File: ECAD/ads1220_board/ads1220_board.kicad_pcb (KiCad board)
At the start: 4 copper layers, 38 x 24 mm, 32 parts, among them J2 LOAD CELL, J3 Conn_01x08, U1 TPS79301-EP, U3 ADS1220xPW, U4 OPA333xxDBV

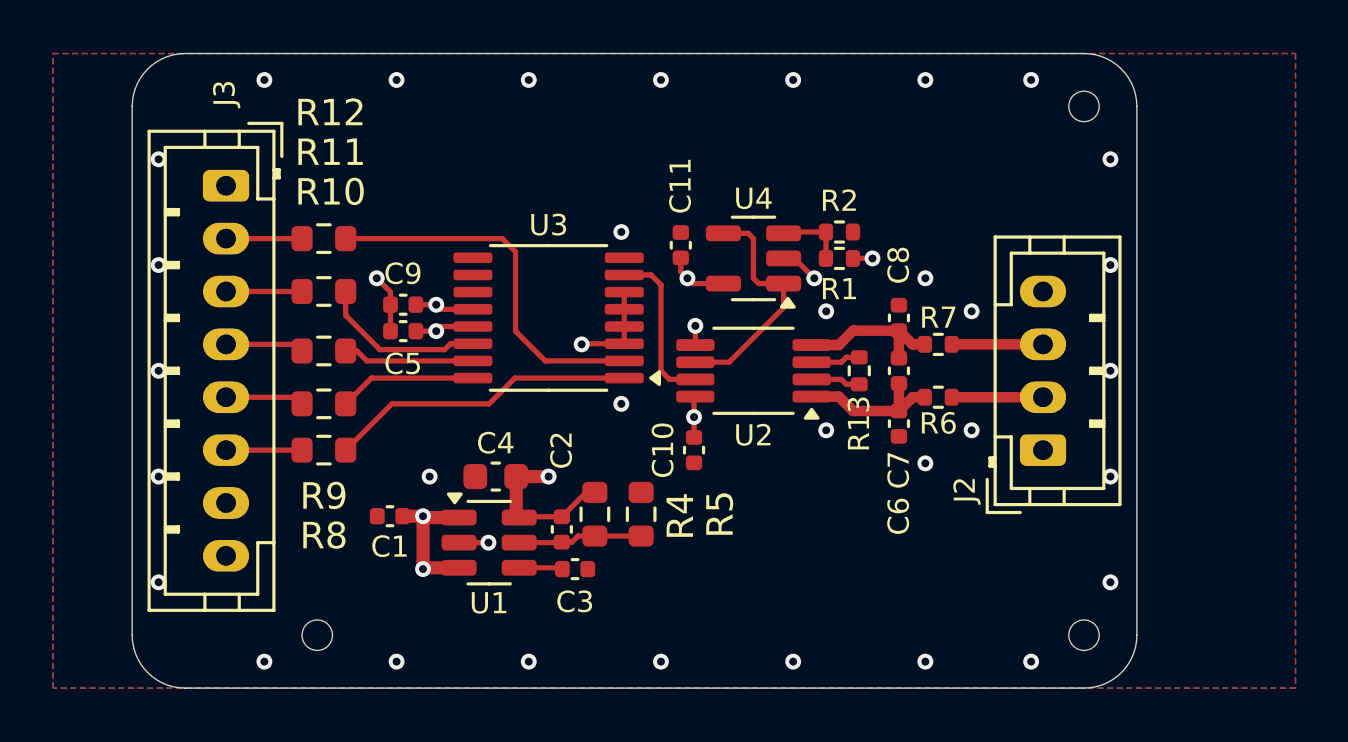
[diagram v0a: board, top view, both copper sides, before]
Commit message: update ads1220 schematic
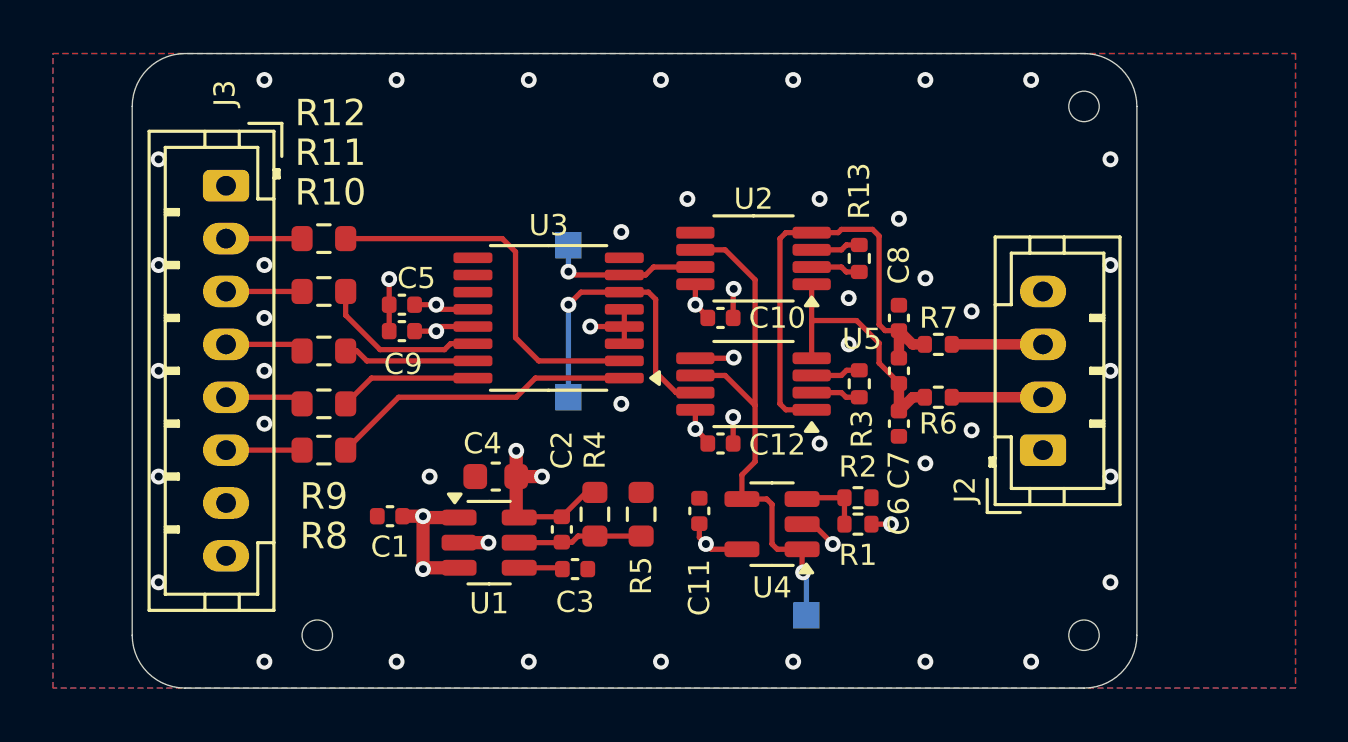
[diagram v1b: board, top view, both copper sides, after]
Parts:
- added C12: 0.1uF, Capacitor_SMD:C_0402_1005Metric, F.Cu at (132.2, 84.8)
- added R3: 220R, Resistor_SMD:R_0402_1005Metric, F.Cu at (137.5, 82.5)
- added TP1: TestPoint, TestPoint:TestPoint_Pad_1.0x1.0mm, B.Cu at (126.5, 77.2)
- added TP2: TestPoint, TestPoint:TestPoint_Pad_1.0x1.0mm, B.Cu at (126.5, 83.0)
- added TP3: TestPoint, TestPoint:TestPoint_Pad_1.0x1.0mm, B.Cu at (135.5, 91.2)
- added U5: ~, Package_SO:Texas_S-PDSO-G8_3x3mm_P0.65mm, F.Cu at (133.5, 82.5)
- moved C11 10.1 mm to (131.4, 87.3)
- moved R1 10.1 mm to (137.4, 87.8)
- moved R2 10.1 mm to (137.4, 86.8)
- moved U4 10.1 mm to (134.2, 87.8)
- moved C10 5.10 mm to (132.2, 80.0), turned to 180 degrees
- moved R13 4.25 mm to (137.5, 77.8)
- moved U2 4.25 mm to (133.5, 77.8)
- moved C5 1.00 mm to (120.2, 79.5)
- moved C9 1.00 mm to (120.2, 80.5)
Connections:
- C9 pad 2: +4V -> +3V3
- U3 pad 13: +4V -> +3V3
- U3 pad 6: GND -> /SIG_AMP-
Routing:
- net +3V3: track 0.00 -> 12.9 mm, vias 0 -> 1
- net /SIG_FLTR-: track 5.76 -> 18.0 mm
- net /INA_REF: track 9.05 -> 20.5 mm, vias 0 -> 1
- net /SIG_AMP-: track 0.00 -> 11.3 mm, vias 0 -> 1
- net /SIG_FLTR+: track 5.76 -> 9.75 mm
- net Net-(R3-Pad2): track 0.00 -> 1.88 mm
- net Net-(R3-Pad1): track 0.00 -> 1.87 mm
- net GND: track 9.10 -> 10.7 mm, vias 38 -> 48
- net /SIG_AMP+: track 6.23 -> 5.98 mm, vias 0 -> 1
- net +4V: track 15.5 -> 15.3 mm, vias 6 -> 7
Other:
- board text added: "ADC: ADS1220 REG: TPS791 INST_AMP: INA827 OP_AMP: OPA333"
- board text added: "INS_REF"
- board text added: "LOAD CELL"
- board text added: "REV B T.W."
- board text added: "SIG_AMP+"
- board text added: "SIG_AMP-"
- board text removed: "LOAD CELL ADC: ADS1220 REG: TPS791 INST_AMP: INA827 OP_AMP: OPA333 REVA T.W."

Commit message: change from 2 ina to 1
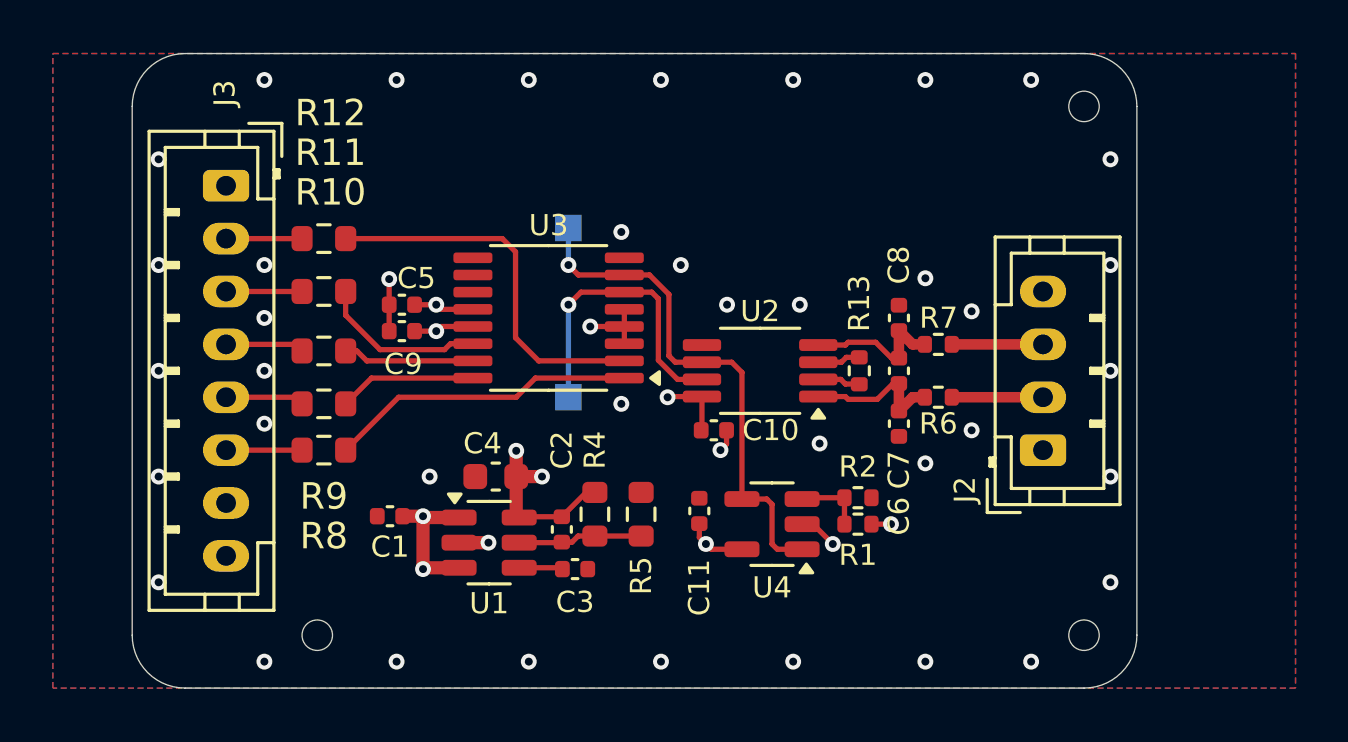
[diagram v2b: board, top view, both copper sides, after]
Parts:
- removed C12: 0.1uF, Capacitor_SMD:C_0402_1005Metric
- removed R3: 220R, Resistor_SMD:R_0402_1005Metric
- removed TP3: TestPoint, TestPoint:TestPoint_Pad_1.0x1.0mm
- removed U5: ~, Package_SO:Texas_S-PDSO-G8_3x3mm_P0.65mm
- U2: value ~ -> INA826
- moved TP2 6.40 mm to (126.5, 76.6)
- moved TP1 5.75 mm to (126.5, 83.0)
- moved C10 4.26 mm to (132.0, 84.2)
- moved U2 4.26 mm to (133.8, 82.0)
- moved R13 4.25 mm to (137.5, 82.0)
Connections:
- TP2 pad 1: /SIG_AMP- -> /INA_REF
- U3 pad 6: /SIG_AMP- -> /SIG_AMP+
- U3 pad 7: /SIG_AMP+ -> /INA_REF
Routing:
- net /SIG_FLTR-: track 18.0 -> 5.58 mm
- net /SIG_AMP-: track 11.3 -> 0.00 mm, vias 1 -> 0
- net /SIG_AMP+: track 5.98 -> 11.1 mm
- net /SIG_FLTR+: track 9.75 -> 5.58 mm
- net GND: track 10.7 -> 8.01 mm, vias 48 -> 44
- net Net-(R3-Pad2): track 1.88 -> 0.00 mm
- net Net-(R3-Pad1): track 1.87 -> 0.00 mm
- net /INA_REF: track 20.5 -> 19.3 mm
- net +4V: track 15.3 -> 15.0 mm, vias 7 -> 6

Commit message: update, add second sensor
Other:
- board text removed: "INS_REF"
